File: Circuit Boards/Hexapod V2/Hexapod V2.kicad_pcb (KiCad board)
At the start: 4 copper layers, 34 parts, among them J1 Screw_Terminal_01x02, J2 Conn_01x14_Pin, U1 MPU6050, U2 NRF24L01_Breakout, U3 YAAJ_DCDC_StepDown_LM2596

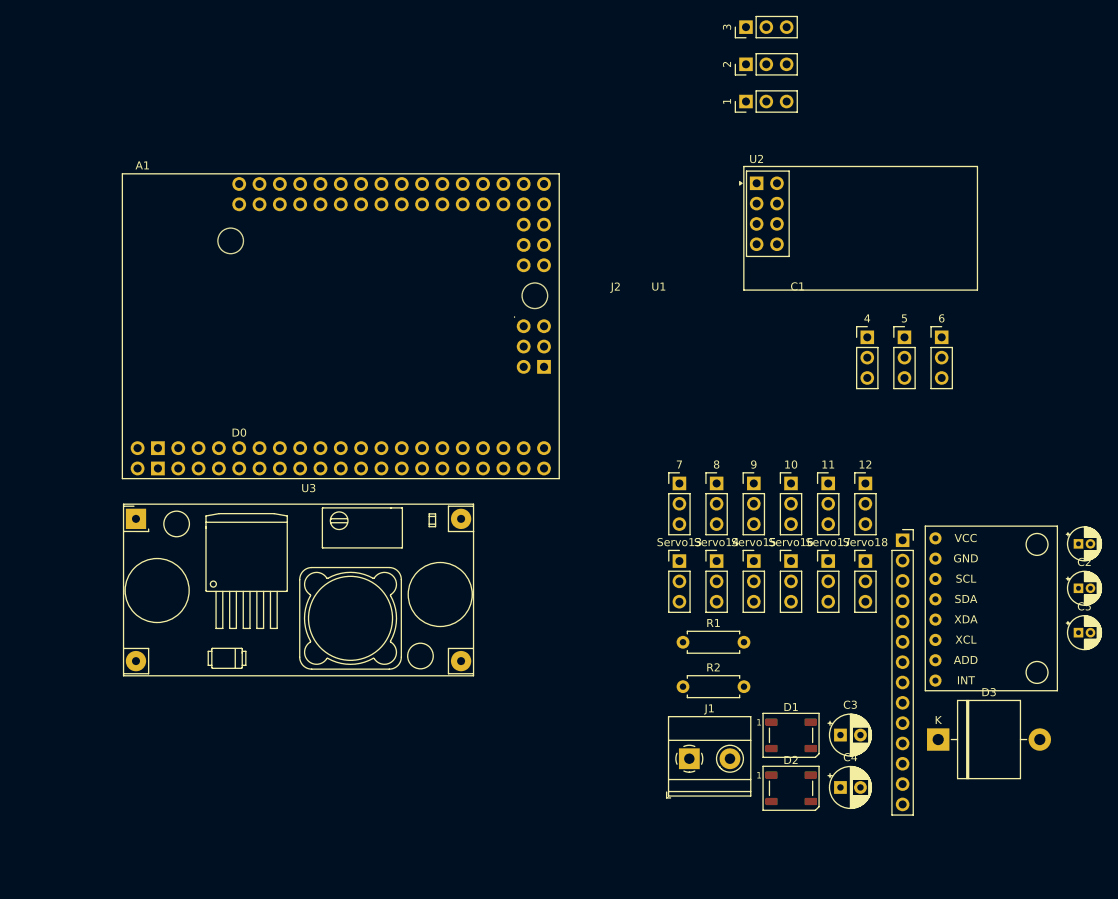
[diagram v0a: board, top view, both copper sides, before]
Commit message: Started Firmware + Continued PCB
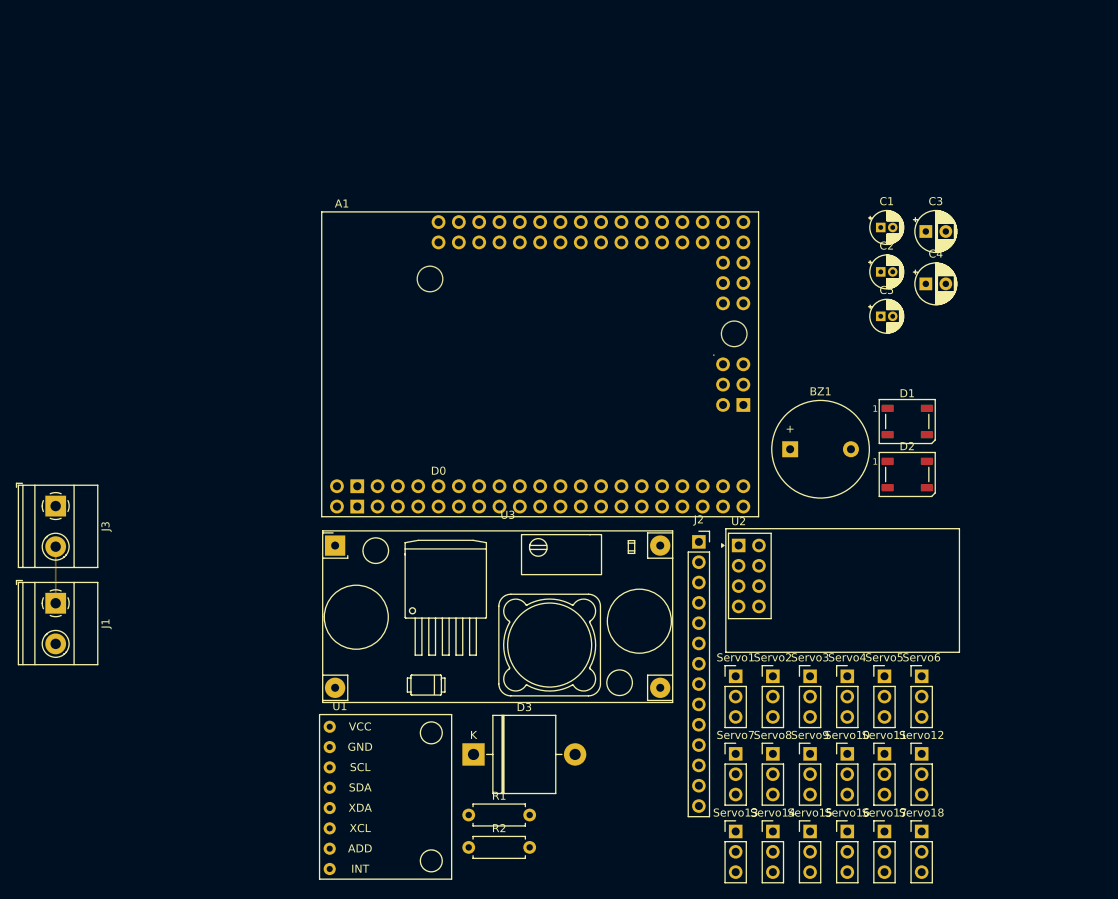
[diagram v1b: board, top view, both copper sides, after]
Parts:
- removed 1, 10, 11, 12, 2, 3, 4, 5, 6, 7, 8, 9: Conn_01x03_Pin, Connector_PinHeader_2.54mm:PinHeader_1x03_P2.54mm_Vertical
- added BZ1: Buzzer, Buzzer_Beeper:Buzzer_12x9.5RM7.6, F.Cu at (163.6, 81.6)
- added J3: Switch, TerminalBlock_Phoenix:TerminalBlock_Phoenix_MKDS-1,5-2-5.08_1x02_P5.08mm_Horizontal, F.Cu at (71.8, 88.7)
- added Servo1: Conn_01x03_Pin, Connector_PinHeader_2.54mm:PinHeader_1x03_P2.54mm_Vertical, F.Cu at (156.8, 110.0)
- added Servo10: Conn_01x03_Pin, Connector_PinHeader_2.54mm:PinHeader_1x03_P2.54mm_Vertical, F.Cu at (170.7, 119.7)
- added Servo11: Conn_01x03_Pin, Connector_PinHeader_2.54mm:PinHeader_1x03_P2.54mm_Vertical, F.Cu at (175.3, 119.7)
- added Servo12: Conn_01x03_Pin, Connector_PinHeader_2.54mm:PinHeader_1x03_P2.54mm_Vertical, F.Cu at (180.0, 119.7)
- added Servo2: Conn_01x03_Pin, Connector_PinHeader_2.54mm:PinHeader_1x03_P2.54mm_Vertical, F.Cu at (161.4, 110.0)
- added Servo3: Conn_01x03_Pin, Connector_PinHeader_2.54mm:PinHeader_1x03_P2.54mm_Vertical, F.Cu at (166.1, 110.0)
- added Servo4: Conn_01x03_Pin, Connector_PinHeader_2.54mm:PinHeader_1x03_P2.54mm_Vertical, F.Cu at (170.7, 110.0)
- added Servo5: Conn_01x03_Pin, Connector_PinHeader_2.54mm:PinHeader_1x03_P2.54mm_Vertical, F.Cu at (175.3, 110.0)
- added Servo6: Conn_01x03_Pin, Connector_PinHeader_2.54mm:PinHeader_1x03_P2.54mm_Vertical, F.Cu at (180.0, 110.0)
- added Servo7: Conn_01x03_Pin, Connector_PinHeader_2.54mm:PinHeader_1x03_P2.54mm_Vertical, F.Cu at (156.8, 119.7)
- added Servo8: Conn_01x03_Pin, Connector_PinHeader_2.54mm:PinHeader_1x03_P2.54mm_Vertical, F.Cu at (161.4, 119.7)
- added Servo9: Conn_01x03_Pin, Connector_PinHeader_2.54mm:PinHeader_1x03_P2.54mm_Vertical, F.Cu at (166.1, 119.7)
- C5: value 0.1μF -> 22μF
- J1: value Screw_Terminal_01x02 -> Battery
- U3: value YAAJ_DCDC_StepDown_LM2596 -> Buck Converter
- moved J1 81.6 mm to (71.8, 100.9), turned to -90 degrees
- moved U1 79.3 mm to (106.0, 134.1)
- moved C3 63.8 mm to (180.5, 54.4)
- moved C4 63.8 mm to (180.5, 61.0)
- moved D3 58.1 mm to (124.0, 119.8)
- moved C5 46.6 mm to (174.9, 65.0)
- moved C1 46.6 mm to (174.9, 53.9)
- moved C2 46.6 mm to (174.9, 59.5)
- moved U2 45.3 mm to (157.1, 93.7)
- moved D1 41.8 mm to (178.2, 78.2)
- moved D2 41.8 mm to (178.2, 84.8)
- moved Servo13 34.5 mm to (156.8, 129.4)
- moved Servo14 34.5 mm to (161.4, 129.4)
- moved Servo15 34.5 mm to (166.1, 129.4)
- moved Servo18 34.5 mm to (180.0, 129.4)
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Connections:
- A1 pad A2: unconnected-(A1-PadA2) -> A2
- U3 pad 1: Net-(J1-Pin_2) -> GND
- U3 pad 2: Net-(J1-Pin_1) -> VIN
- U3 pad 3: GND -> Net-(J1-Pin_2)
- U3 pad 4: VIN -> Net-(J3-Pin_1)
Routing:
- net Net-(J1-Pin_1): track 0.00 -> 7.07 mm
